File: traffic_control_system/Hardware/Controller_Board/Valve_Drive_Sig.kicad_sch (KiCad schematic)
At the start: 56 parts, among them U10 MC74HC238A, U11 74LVC2G04W6-7, U12 74LVC2G04W6-7, U13 74LVC2G04W6-7, U14 74LVC2G04W6-7, U15 74LVC2G04W6-7, U16 74LVC2G04W6-7, U17 74LS08, U18 74LVC2G04W6-7, U19 74LVC2G04W6-7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

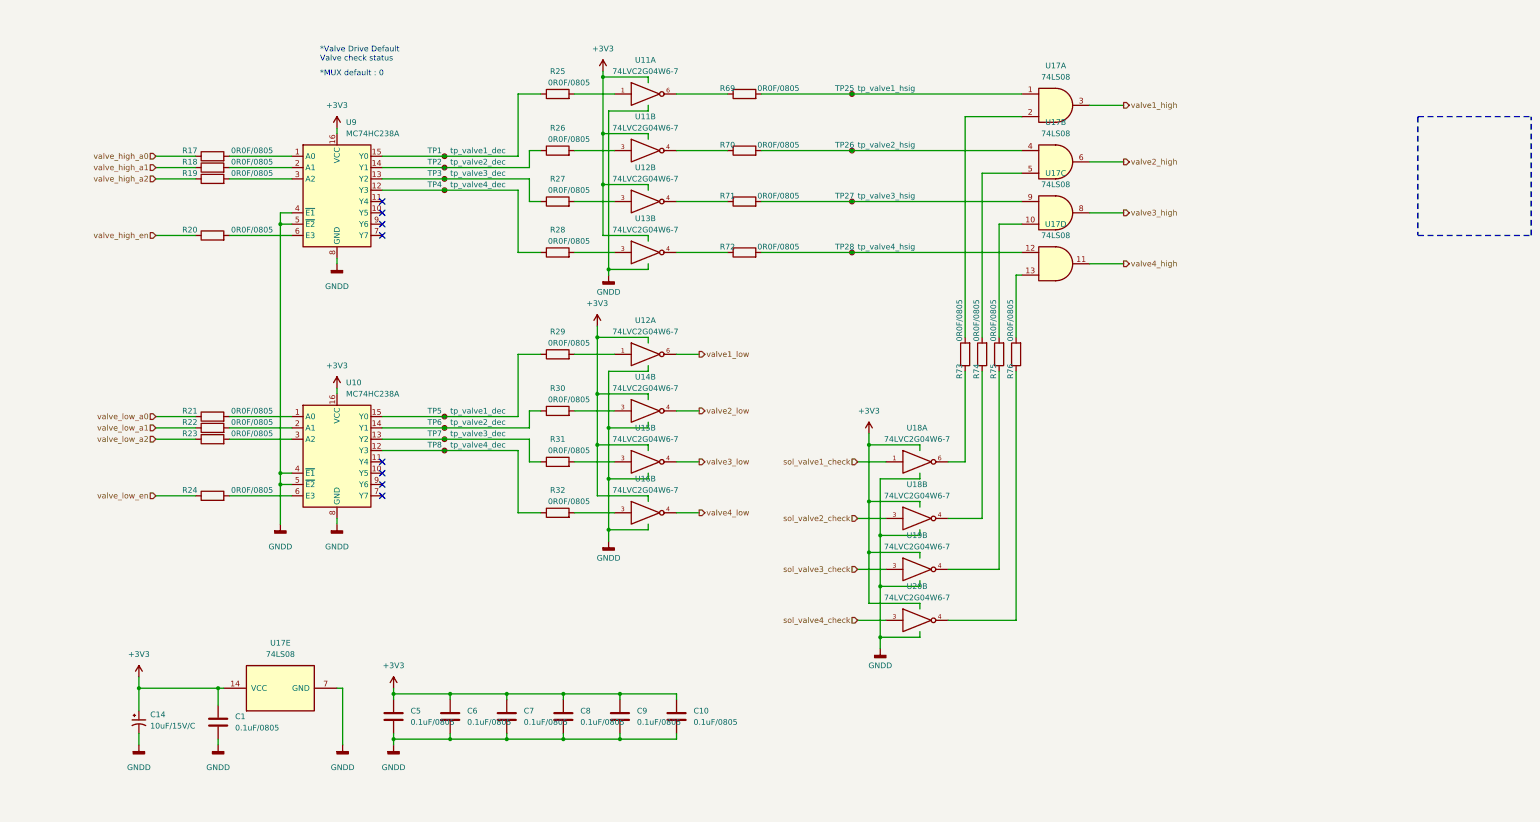
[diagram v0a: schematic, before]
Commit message: issue : 밸브체크 회로 다이오드 누락 추가[ISSUE-6]
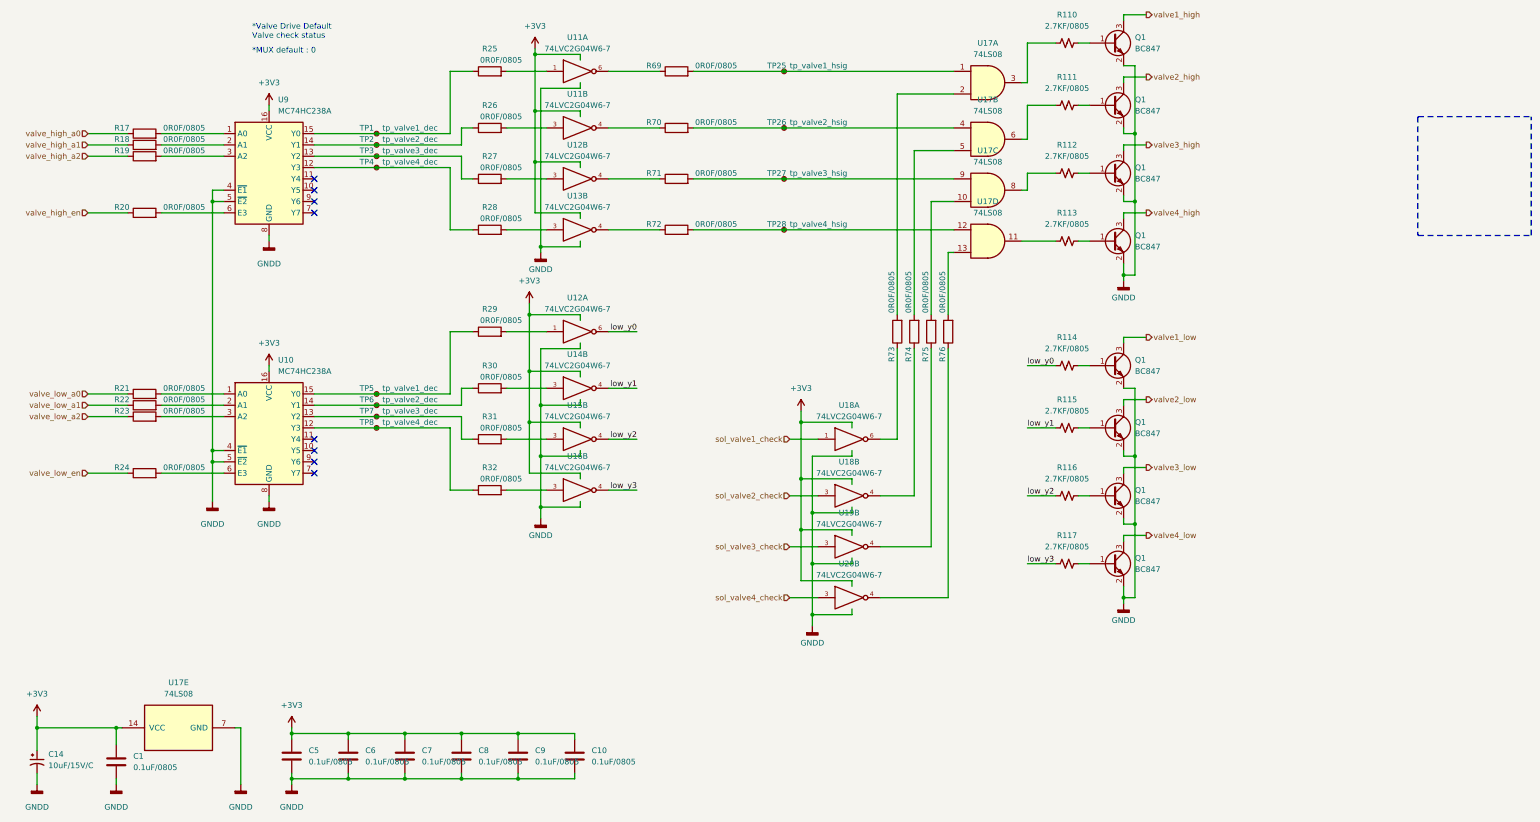
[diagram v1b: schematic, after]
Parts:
- added Q1 (x8): BC847, symbol Transistor_BJT:BC847
- added R110, R111, R112, R113, R114, R115, R116, R117: 2.7KF/0805, symbol Device:R_Small_US
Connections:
- net GND: now also Q1.2 (E), Q1.2 (E), Q1.2 (E), Q1.2 (E), Q1.2 (E), Q1.2 (E), Q1.2 (E), Q1.2 (E)
- net valve1_high: now also Q1.3 (C); no longer U17.3
- net valve1_low: now also Q1.3 (C); no longer U12.6
- net valve2_high: now also Q1.3 (C); no longer U17.6
- net valve2_low: now also Q1.3 (C); no longer U14.4
- net valve3_high: now also Q1.3 (C); no longer U17.8
- net valve3_low: now also Q1.3 (C); no longer U15.4
- net valve4_high: now also Q1.3 (C); no longer U17.11
- net valve4_low: now also Q1.3 (C); no longer U16.4
- new net: R110.1, U17.3
- new net: Q1.1 (B), R117.2
- new net: Q1.1 (B), R112.2
- new net: R113.1, U17.11
- new net: Q1.1 (B), R113.2
- new net: Q1.1 (B), R111.2
- new net: Q1.1 (B), R115.2
- new net: R111.1, U17.6
- new net: R112.1, U17.8
- new net: Q1.1 (B), R114.2
- new net: Q1.1 (B), R116.2
- new net: Q1.1 (B), R110.2
- new net low_y0: R114.1, U12.6
- new net low_y1: R115.1, U14.4
- new net low_y2: R116.1, U15.4
- new net low_y3: R117.1, U16.4
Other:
- title: (none) -> Valve_Drive_Sig
- moved on the sheet: C1, C10, C14, C5, C6, C7, C8, C9, R17, R18, R19, R20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
